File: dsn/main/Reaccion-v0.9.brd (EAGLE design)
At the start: 100 x 80 mm, 135 parts, among them J1 U.FL, Q1 2N7002K-T1-E3, Q3 2N7002K-T1-E3, Q9 SI2301CDS, T1 BC847, T2 BC847

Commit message: PCB re-design
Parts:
- removed C12: T491A336K004AT, custom_componentsv0.9:3216-18
- removed C13: EDK105M050A9BAA, custom_componentsv0.9:EDK105M050A9BAA
- removed C26, CS, CS1: 1uF, SparkFun-Capacitors:0805
- removed CF1, CF2, CF3: 39pF, SparkFun-Capacitors:0805
- removed D1, D2, D3: MBRS140T3-D, custom_componentsv0.9:MBRS140T3G
- removed IC_14: MAX7313AEG, maxim:QSOP24
- removed IC_2, IC_4, IC_5: LM2621, custom_componentsv0.9:R-PDSO-G8
- removed JP4: GPIO, SparkFun-Connectors:2X10
- removed JP5: POWER_JACKPTH, SparkFun-Connectors:POWER_JACK_PTH
- removed L4, L5, L7: NR4018T6R8M, custom_componentsv0.9:NR4018/NRS4018
- removed R29, R30, R31, R32, R33, R34, R35, R39, R40, R41, R48: 4.7K, SparkFun-Resistors:0805
- removed RF1, RF3, RF5: 150K, SparkFun-Resistors:0805
- removed RF2: 91K, SparkFun-Resistors:0805
- removed RF4: 50K, SparkFun-Resistors:0805
- removed RF6: 16K, SparkFun-Resistors:0805
- removed RFQ, RFQ1, RFQ2: 160K, SparkFun-Resistors:0805
- removed SJ4: SOLDERJUMPERNO, SparkFun-Retired:SJ_2S-NO
- removed SJ5, SJ6: SOLDERJUMPERTRACE, SparkFun-Retired:SJ_2S-TRACE
- added CIN, CIN1: 100uF, custom_componentsv0.9:1210-POLARIZED
- added DOUT, DOUT1: SD1206S040S2R0, custom_componentsv0.9:1206-POL
- added JP6: USB-B, SparkFun-Connectors:USB-B-PTH
- added R13: 30K, SparkFun-Resistors:0805
- added R14, R21: 10K, SparkFun-Resistors:0805
- added R15: 84.5K, SparkFun-Resistors:0805
- added U$1, U$2: LT1935ES5, custom_componentsv0.9:SOT23-5
- added U1: MIC5219 3.3V, SparkFun-PowerIC:SOT23-5
- BAT1: value (none) -> 3.7V
- C1: value T491A336K004AT -> 0.22uF; device custom_componentsv0.9:3216-18 -> SparkFun-Capacitors:0805
- C11: value T491A686K004AT -> 470pF; device custom_componentsv0.9:3216-18 -> SparkFun-Capacitors:0805
- C2: value T491A686K004AT -> 68pF; device custom_componentsv0.9:3216-18 -> SparkFun-Capacitors:0805
- C3: value EDK105M050A9BAA -> 22uF; device custom_componentsv0.9:EDK105M050A9BAA -> SparkFun-Capacitors:0805
- C4: value T491A686K004AT -> 0.22uF; device custom_componentsv0.9:3216-18 -> SparkFun-Capacitors:0805
- C5: value T491A336K004AT -> 68pF; device custom_componentsv0.9:3216-18 -> SparkFun-Capacitors:0805
- C6: value EDK105M050A9BAA -> 47uF; device custom_componentsv0.9:EDK105M050A9BAA -> SparkFun-Capacitors:0805
- L3, L6: value NR4018T6R8M -> 1.8uH; device custom_componentsv0.9:NR4018/NRS4018 -> inductor-bourns:SRR4028
- R1, R2: value 500 -> 10K
- moved C11 20.8 mm to (21.6, 34.0), turned to 90 degrees
- moved C1 18.7 mm to (31.5, 15.6), turned to 0 degrees
- moved C4 16.4 mm to (12.9, 29.7), turned to 90 degrees
- moved C3 15.4 mm to (29.5, 4.80), turned to 180 degrees
- moved L3 13.7 mm to (23.4, 7.00), turned to 90 degrees
- moved IC_17 13.5 mm to (44.9, 53.4), flipped to the top
- moved IC_10 12.0 mm to (81.4, 34.0)
- moved L6 11.5 mm to (21.6, 21.6), turned to 180 degrees
- moved IC_18 11.2 mm to (32.6, 53.3), flipped to the top
- moved C6 10.8 mm to (23.8, 27.5), turned to 270 degrees
- moved S1 10.0 mm to (50.0, 40.0)
- moved D4 9.68 mm to (11.6, 14.1), turned to 0 degrees
- moved C19 9.51 mm to (18.4, 66.0)
- moved C2 9.29 mm to (31.5, 11.7), turned to 180 degrees
- moved R42 9.23 mm to (45.9, 40.2), turned to 270 degrees
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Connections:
- removed net 1V8_EN: IC_13.18, IC_3.3, R34.2
- removed net 1V8_TRANS_EN: IC_13.19, IC_17.8, IC_18.8, R33.2
- removed net 2V8_TRANS_EN: IC_10.8, IC_13.20, R32.2
- removed net BT_RESET: IC_13.5, IC_15.11, R40.2
- removed net GPIO1: IC_14.5, JP4.3
- removed net GPIO10: IC_14.15, JP4.13
- removed net GPIO11: IC_14.16, JP4.14
- removed net GPIO12: IC_14.17, JP4.15
- removed net GPIO13: IC_14.18, JP4.16
- removed net GPIO14: IC_14.19, JP4.17
- removed net GPIO15: IC_14.20, JP4.18
- removed net GPIO2: IC_14.6, JP4.5
- removed net GPIO3: IC_14.7, JP4.6
- removed net GPIO4: IC_14.8, JP4.7
- removed net GPIO5: IC_14.9, JP4.8
- removed net GPIO6: IC_14.10, JP4.9
- removed net GPIO7: IC_14.11, JP4.10
- removed net GPIO8: IC_14.13, JP4.11
- removed net GPIO9: IC_14.14, JP4.12
- removed net IO_INT1: IC_12.33, IC_14.1
- removed net N$10: CS1.2, D2.1, L7.P$2
- removed net N$16: IC_5.3, RFQ2.1
- removed net N$17: CF3.1, IC_5.4, RF5.2, RF6.1
- removed net N$40: IC_14.21, R29.1, SJ4.2
- removed net N$41: IC_14.2, R30.1, SJ5.2
- removed net N$42: IC_14.3, R31.1, SJ6.2
- removed net N$7: CS.2, D1.1, L4.P$2
- removed net N$9: CF2.1, IC_4.4, RF3.2, RF4.1
- removed net W: C20.2, R18.2
- net 12V: now also C2.1, C3.1, DOUT1.2, R15.1; no longer C11.1, CF3.2, D3.2, RF5.1
- net 12V_EN: now also IC_12.26, R1.1; no longer IC_5.2, R35.2
- net 3V3: now also U1.5; no longer C2.1, C26.2, CF1.2, D1.2, IC_10.14, IC_14.24, IC_17.14, IC_18.14, IC_3.1, JP1.9, JP2.1, JP4.4, R29.2, R3.2, R30.2, R31.2, R32.1, R33.1, R34.1, R35.1, R39.1, R40.1, R41.1, R48.1, R5.2, RF1.1
- net 5V: now also C5.1, C6.1, DOUT.2, IC_10.14, IC_10.8, IC_17.14, IC_17.8, IC_18.14, IC_18.8, IC_3.1, IC_3.3, JP1.9, JP2.1, R13.1, R3.2, R5.2, U1.1, U1.3; no longer C4.1, C7.2, CF2.2, D2.2, IC_6.4, JP4.1, JP4.2, RF3.1
- net BT_CMD: now also IC_12.33, IC_15.26; no longer IC_13.6, R39.2
- net BT_EN: now also IC_12.27; no longer IC_13.4, R41.2
- net GND: now also C11.1, C3.2, C6.2, CIN.2, CIN1.2, JP6.GND, R14.2, R21.2, U$1.2, U$2.2, U1.2; no longer C11.2, C12.2, C13.P$2, C2.2, C26.1, C3.P$2, C5.2, C6.P$2, IC_14.12, IC_2.1, IC_2.5, IC_4.1, IC_4.5, IC_5.1, IC_5.5, JP4.19, JP4.20, JP5.GND, JP5.GNDBREAK, L4.P$1, L7.P$1, RF2.2, RF4.2, RF6.2, SJ4.1, SJ5.1, SJ6.1
- net N$1: now also DOUT1.1, L3.2, U$2.1; no longer CS.1, IC_2.8, L3.P$2
- net N$14: now also IC_12.29; no longer D3.1, IC_5.8, L5.P$2
- net N$2: now also DOUT.1, L6.2, U$1.1; no longer CS1.1, IC_4.8, L6.P$2
- net N$3: now also C1.1, R1.2, U$2.4; no longer C3.P$1, IC_2.2, IC_2.6, R1.1, RFQ.2
- net N$4: now also C11.2, U1.4; no longer IC_2.3, RFQ.1
- net N$5: now also C2.2, R15.2, R21.1, U$2.3; no longer CF1.1, IC_2.4, RF1.2, RF2.1
- net N$6: now also C5.2, R13.2, R14.1, U$1.3; no longer C6.P$1, IC_4.2, IC_4.6, R2.1, RFQ1.2
- net N$8: now also C4.1, R2.2, U$1.4; no longer IC_4.3, RFQ1.1
- net SCL: no longer IC_14.22
- net SDA: no longer IC_14.23
- net SIM_DATA: now also C20.2, R18.2
- net VEXT: now also C7.2, IC_6.4, JP6.VBUS; no longer JP5.PWR
- net VIN: now also CIN.1, CIN1.1, L3.1, L6.1, R2.1, U$1.5, U$2.5; no longer C1.1, C12.1, C13.P$1, C5.1, IC_2.7, IC_4.7, IC_5.6, IC_5.7, L3.P$1, L5.P$1, L6.P$1, R1.2, R2.2, RFQ2.2
- net XBEE_RESET: now also IC_12.28; no longer IC_14.4, R48.2
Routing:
- net GND: track 8.37 -> 1008.3 mm, vias 72 -> 45
- net 3V3: track 437.5 -> 206.5 mm, vias 14 -> 9
- net 5V: track 103.8 -> 275.9 mm, vias 4 -> 5
- net 1V8_TRANS_EN: track 149.2 -> 0.00 mm, vias 9 -> 0
- net 1V8_EN: track 147.3 -> 0.00 mm, vias 8 -> 0
- net SIM_DATA: track 0.00 -> 75.4 mm, vias 0 -> 5
- net W: track 63.5 -> 0.00 mm, vias 3 -> 0
- net BT_RESET: track 55.5 -> 0.00 mm, vias 4 -> 0
- net VIN: track 112.5 -> 57.0 mm
- net 2V8_TRANS_EN: track 49.9 -> 0.00 mm, vias 6 -> 0
- net 12V: track 104.1 -> 142.6 mm, vias 2 -> 5
- net IO_INT1: track 28.3 -> 0.00 mm, vias 2 -> 0
- net SIM900_PWR: track 83.0 -> 55.7 mm
- net SCL: track 105.7 -> 81.8 mm, vias 7 -> 3
- net SPI1_MISO: track 60.4 -> 37.0 mm, vias 1 -> 0
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- added copper zone on layer 1, net N$2
- removed copper zone on layer 16, net GND

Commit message: Laen's DRC corrections, small modifications
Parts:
- JP2: device SparkFun-Connectors:AVR_ICSP -> pinhead:2X05
- turned JP2 to 270 degrees
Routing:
- net N$37: track 7.29 -> 13.2 mm
- net SDA: track 75.8 -> 77.0 mm
- added copper zone on layer 16, net GND

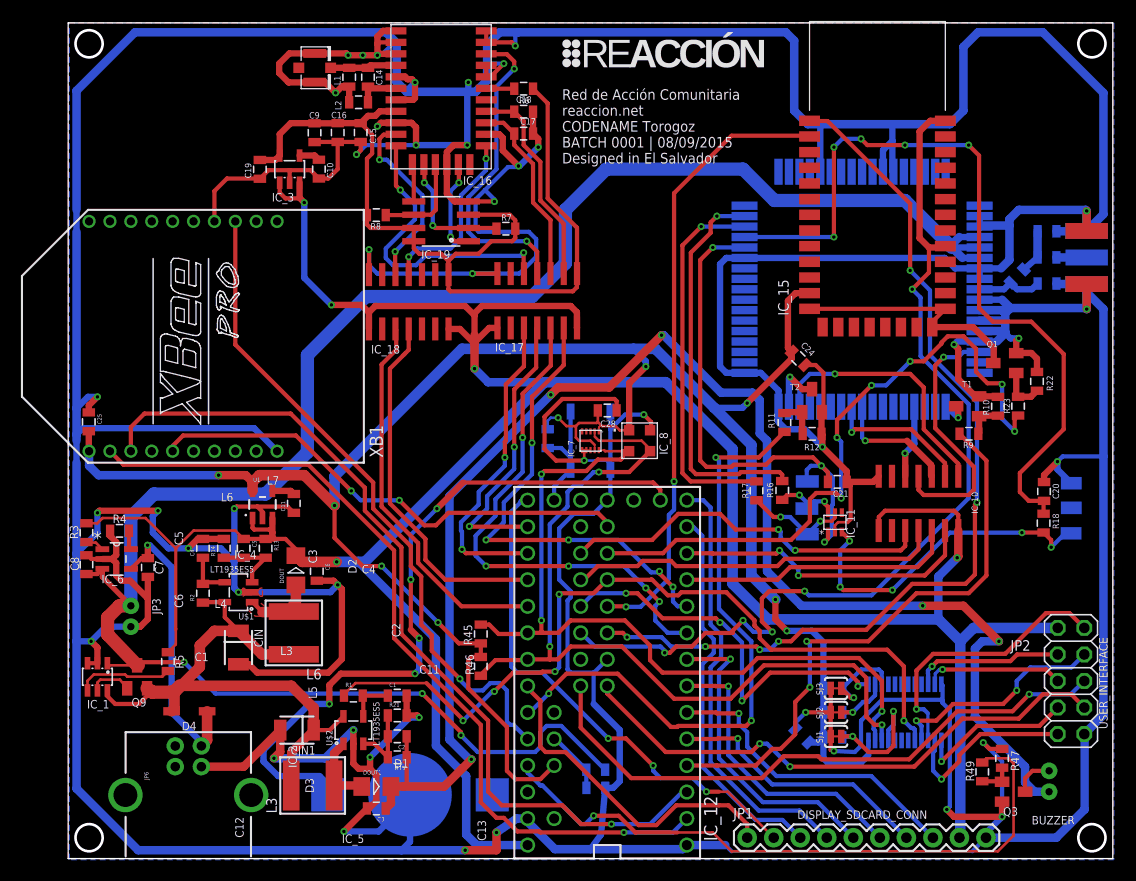
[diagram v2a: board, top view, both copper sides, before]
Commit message: Added power source corrections
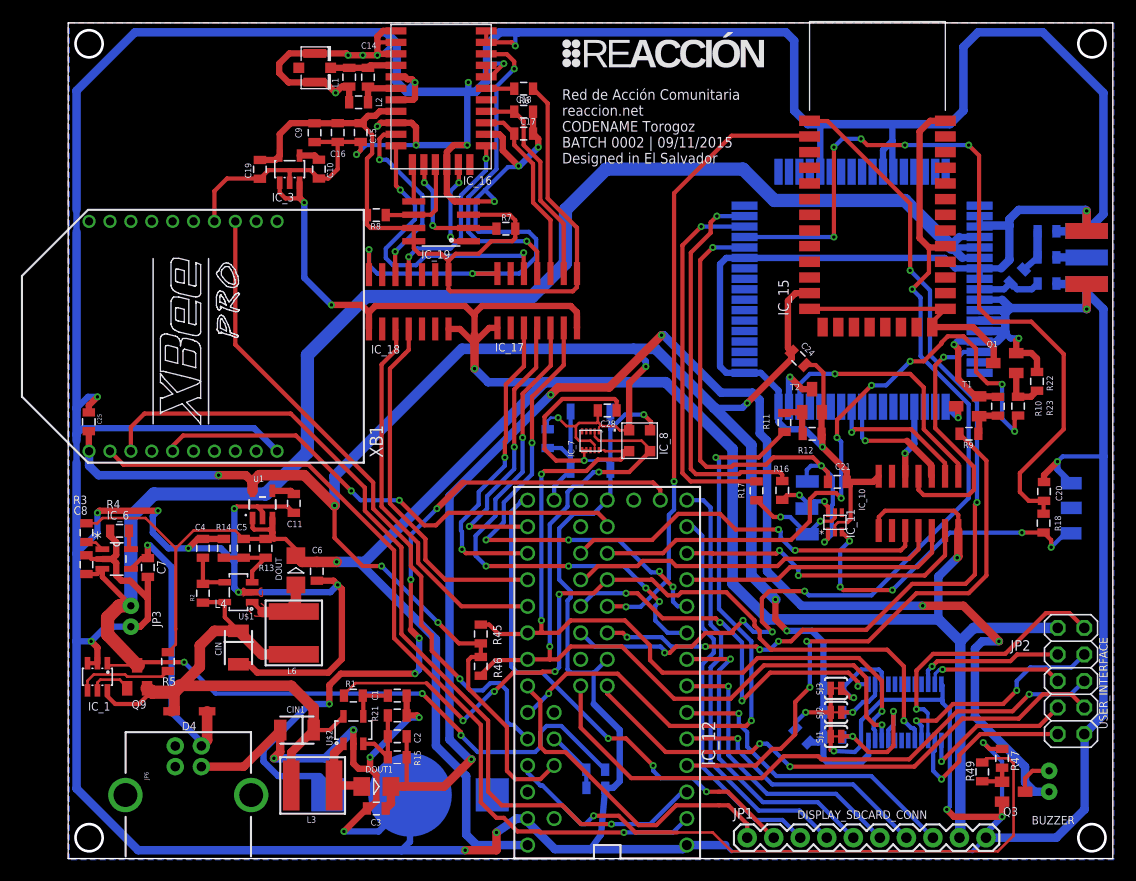
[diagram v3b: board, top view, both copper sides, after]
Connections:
- removed net N$14: IC_12.29
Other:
- board text added: "Red de Acción Comunitaria reaccion.net CODENAME Torogoz BATCH 0002 | 09/11/2015 Designed in El Salvador"
- board text removed: "C1"
- board text removed: "C11"
- board text removed: "C12"
- board text removed: "C13"
- board text removed: "C2"
- board text removed: "C3"
- board text removed: "C4"
- board text removed: "C5"
- board text removed: "C6"
- board text removed: "D1"
- board text removed: "D2"
- board text removed: "D3"
- board text removed: "IC_2"
- board text removed: "IC_4"
- board text removed: "IC_5"
- board text removed: "L3"
- board text removed: "L5"
- board text removed: "L6"
- board text removed: "L7"
- board text removed: "Red de Acción Comunitaria reaccion.net CODENAME Torogoz BATCH 0001 | 08/09/2015 Designed in El Salvador"

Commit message: Initial release for Prototipo1
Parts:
- IC_7: device Reaccion-Custom:2X2-DFN -> Reaccion-Custom-revised:2X2-DFN
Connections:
- net 3V3: now also IC_7.8; no longer IC_7.9
- net BT_RX: now also IC_12.21/A7; no longer IC_12.25
- net BT_TX: now also IC_12.20/A6; no longer IC_12.24
- net CHG_STAT: now also IC_13.5
- net DISPLAY_BL: now also IC_12.24; no longer IC_12.20/A6
- net GND: now also IC_7.9; no longer IC_7.8
- net PWR_STAT: now also IC_13.4
- net SIM900_RESET: now also IC_12.25; no longer IC_12.21/A7
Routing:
- net DISPLAY_BL: track 32.1 -> 8.85 mm
- net SIM900_RESET: track 59.5 -> 49.3 mm, vias 3 -> 2
- net BT_TX: track 90.0 -> 84.6 mm, vias 6 -> 5
- net BT_RX: track 60.6 -> 57.4 mm, vias 2 -> 1
- net GND: track 1008.7 -> 1009.9 mm
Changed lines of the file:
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@@
 <setting verticaltext="up"/>
 </settings>
-<grid distance="0.1" unitdist="mm" unit="mm" style="lines" multiple="1" display="yes" altdistance="0.1" altunitdist="mm" altunit="mm"/>
+<grid distance="0.01" unitdist="mm" unit="mm" style="lines" multiple="1" display="yes" altdistance="0.01" altunitdist="mm" altunit="mm"/>
 <layers>
 <layer number="1" name="Top" color="4" fill="1" visible="yes" active="yes"/>
@@
 <attribute name="NAME" x="57.41" y="38.67" size="0.8128" layer="25" font="fixed" rot="R90"/>
 </element>
-<element name="IC_7" library="Reaccion-Custom" package="2X2-DFN" value="MMA8653FC" x="50" y="40" smashed="yes" rot="R270">
+<element name="IC_7" library="Reaccion-Custom-revised" package="2X2-DFN" value="MMA8653FC" x="50" y="40" smashed="yes" rot="R270">
 <attribute name="NAME" x="48.45" y="38.44" size="0.6096" layer="21" font="fixed" rot="R90"/>
 </element>
@@
 <contactref element="R47" pad="1"/>
 <contactref element="Q3" pad="2"/>
-<contactref element="IC_7" pad="8"/>
+<contactref element="IC_7" pad="9"/>
 <contactref element="IC_7" pad="7"/>
 <contactref element="IC_7" pad="6"/>
@@
 <wire x1="49.4" y1="38.9025" x2="49.2" y2="39.1025" width="0.254" layer="1"/>
 <wire x1="49.6" y1="39.1025" x2="49.2" y2="39.1025" width="0.254" layer="1"/>
-<wire x1="50" y1="39.1025" x2="49.6" y2="39.1025" width="0.1524" layer="1"/>
 <wire x1="51.905" y1="42.794" x2="51.905" y2="41.1" width="0.4064" layer="16"/>
 <wire x1="51.905" y1="41.1" x2="51.905" y2="37.7" width="0.4064" layer="16"/>
@@
 <wire x1="77.9" y1="15.2" x2="83.6" y2="15.2" width="0.4064" layer="16"/>
 <wire x1="83.6" y1="15.2" x2="83.7" y2="15.1" width="0.4064" layer="16"/>
+<wire x1="50.4" y1="39.1025" x2="50.4" y2="38.77" width="0.1524" layer="1"/>
+<wire x1="50.4" y1="38.77" x2="49.73" y2="38.1" width="0.1524" layer="1"/>
+<wire x1="49.73" y1="38.1" x2="49.4" y2="38.1" width="0.1524" layer="1"/>
 </signal>
 <signal name="VIN">
@@
 <contactref element="R42" pad="1"/>
 <contactref element="IC_7" pad="1"/>
-<contactref element="IC_7" pad="9"/>
+<contactref element="IC_7" pad="8"/>
 <contactref element="IC_8" pad="1"/>
 <contactref element="C25" pad="2"/>
@@
 <wire x1="50.7" y1="42.9" x2="50.7" y2="41.8" width="0.254" layer="1"/>
 <wire x1="50.7" y1="41.8" x2="51.1" y2="41.4" width="0.254" layer="1"/>
-<wire x1="50.4" y1="39.1025" x2="50.4" y2="39.6" width="0.1524" layer="1"/>
-<wire x1="50.4" y1="39.6" x2="50" y2="40" width="0.254" layer="1"/>
-<wire x1="50" y1="40" x2="48.9" y2="40" width="0.254" layer="1"/>
 <wire x1="48.9" y1="40" x2="48.6" y2="40.3" width="0.254" layer="1"/>
 <wire x1="48.6" y1="40.3" x2="48.6" y2="41.4" width="0.254" layer="1"/>
@@
 <wire x1="71.2" y1="21.8" x2="72.3" y2="20.7" width="0.6096" layer="16"/>
 <wire x1="72.3" y1="20.7" x2="72.3" y2="16.3" width="0.6096" layer="16"/>
+<wire x1="48.9" y1="40" x2="49.7" y2="40" width="0.254" layer="1"/>
+<wire x1="49.7" y1="40" x2="50" y2="39.7" width="0.1524" layer="1"/>
+<wire x1="50" y1="39.7" x2="50" y2="39.1025" width="0.1524" layer="1"/>
 </signal>
 <signal name="5V">
@@
 <wire x1="3.270853125" y1="29.61825625" x2="2.651771875" y2="30.2373375" width="0.254" layer="1"/>
 <wire x1="2.651771875" y1="30.2373375" x2="1.75" y2="30.3" width="0.254" layer="1"/>
+<contactref element="IC_13" pad="5"/>
+<wire x1="3.270853125" y1="29.61825625" x2="79.1475" y2="16.69" width="0" layer="19" extent="1-16"/>
 </signal>
 <signal name="N$11">
@@
 <wire x1="5.65" y1="17.42" x2="9.01500625" y2="17.42" width="0.254" layer="1"/>
 <wire x1="9.01500625" y1="17.42" x2="9.55" y2="17.95499375" width="0.254" layer="1"/>
+<contactref element="IC_13" pad="4"/>
+<wire x1="9.55" y1="17.95499375" x2="78.5125" y2="16.69" width="0" layer="19" extent="1-16"/>
 </signal>
 <signal name="N$13">
@@
 <signal name="SIM900_RESET">
 <contactref element="R11" pad="1"/>
-<contactref element="IC_12" pad="21/A7"/>
-<wire x1="43.98" y1="13.99" x2="44.19" y2="13.99" width="0.4064" layer="16"/>
-<wire x1="44.19" y1="13.99" x2="46" y2="15.8" width="0.4064" layer="16"/>
-<via x="46" y="15.8" extent="1-16" drill="0.3302"/>
-<wire x1="46" y1="15.8" x2="46" y2="16" width="0.4064" layer="1"/>
-<wire x1="46" y1="16" x2="47.7" y2="17.7" width="0.4064" layer="1"/>
-<wire x1="47.7" y1="17.7" x2="52.6" y2="17.7" width="0.4064" layer="1"/>
 <wire x1="57.6" y1="12.7" x2="64.9" y2="12.7" width="0.4064" layer="1"/>
 <wire x1="64.9" y1="12.7" x2="65.4" y2="13.2" width="0.4064" layer="1"/>
@@
 <wire x1="66.115759375" y1="38.4" x2="68.564346875" y2="40.8485875" width="0.4064" layer="1"/>
 <wire x1="52.6" y1="17.7" x2="57.6" y2="12.7" width="0.4064" layer="1"/>
+<contactref element="IC_12" pad="25"/>
+<wire x1="52.6" y1="17.7" x2="51.6" y2="24.15" width="0" layer="19" extent="1-1"/>
 </signal>
 <signal name="SIM900_PWR">
@@
 <signal name="BT_TX">
 <contactref element="IC_15" pad="1"/>
-<contactref element="IC_12" pad="24"/>
-<wire x1="51.6" y1="21.61" x2="53.09" y2="21.61" width="0.4064" layer="1"/>
-<wire x1="53.09" y1="21.61" x2="53.5" y2="21.2" width="0.4064" layer="1"/>
-<via x="53.5" y="21.2" extent="1-16" drill="0.3302"/>
-<wire x1="53.5" y1="21.2" x2="56.8" y2="21.2" width="0.4064" layer="16"/>
 <wire x1="56.8" y1="21.2" x2="57.7" y2="20.3" width="0.4064" layer="16"/>
 <wire x1="57.7" y1="20.3" x2="61" y2="20.3" width="0.4064" layer="16"/>
@@
 <wire x1="82.5" y1="54.4" x2="82.5" y2="48.2" width="0.4064" layer="16"/>
 <wire x1="82.5" y1="48.2" x2="87" y2="43.7" width="0.4064" layer="16"/>
+<contactref element="IC_12" pad="20/A6"/>
+<wire x1="43.98" y1="16.53" x2="56.8" y2="21.2" width="0" layer="19" extent="16-16"/>
 </signal>
 <signal name="BT_RX">
 <contactref element="IC_15" pad="2"/>
-<contactref element="IC_12" pad="25"/>
-<wire x1="51.6" y1="24.15" x2="53.35" y2="24.15" width="0.4064" layer="1"/>
-<wire x1="53.35" y1="24.15" x2="53.4" y2="24.1" width="0.4064" layer="1"/>
-<via x="53.4" y="24.1" extent="1-16" drill="0.3302"/>
-<wire x1="53.4" y1="24.1" x2="54.8" y2="24.1" width="0.4064" layer="16"/>
 <wire x1="54.8" y1="24.1" x2="57.5" y2="26.8" width="0.4064" layer="16"/>
 <wire x1="57.5" y1="26.8" x2="57.5" y2="32.9" width="0.4064" layer="16"/>
@@
 <wire x1="71.5" y1="69" x2="71.09625" y2="69" width="0.4064" layer="1"/>
 <wire x1="71.09625" y1="69" x2="70.969915625" y2="69.126334375" width="0.4064" layer="1"/>
+<contactref element="IC_12" pad="21/A7"/>
+<wire x1="43.98" y1="13.99" x2="54.8" y2="24.1" width="0" layer="19" extent="16-16"/>
 </signal>
 <signal name="BT_CMD">
@@
 <signal name="DISPLAY_BL">
 <contactref element="JP1" pad="1"/>
-<contactref element="IC_12" pad="20/A6"/>
-<wire x1="43.98" y1="16.53" x2="43.98" y2="16.32" width="0.4064" layer="1"/>
-<wire x1="43.98" y1="16.32" x2="45.2" y2="15.1" width="0.4064" layer="1"/>
-<wire x1="45.2" y1="15.1" x2="45.2" y2="10.7" width="0.4064" layer="1"/>
-<wire x1="45.2" y1="10.7" x2="45.7" y2="10.2" width="0.4064" layer="1"/>
-<wire x1="45.7" y1="10.2" x2="47.6" y2="10.2" width="0.4064" layer="1"/>
-<wire x1="47.6" y1="10.2" x2="54.6" y2="3.2" width="0.4064" layer="1"/>
-<wire x1="54.6" y1="3.2" x2="56.3" y2="3.2" width="0.4064" layer="1"/>
-<wire x1="56.3" y1="3.2" x2="58.2" y2="5.1" width="0.4064" layer="1"/>
-<wire x1="58.2" y1="5.1" x2="62.3" y2="5.1" width="0.4064" layer="1"/>
-<wire x1="62.3" y1="5.1" x2="63.2" y2="5.1" width="0.4064" layer="1"/>
+<wire x1="58.2" y1="5.1" x2="63.2" y2="5.1" width="0.4064" layer="1"/>
 <wire x1="63.2" y1="5.1" x2="65" y2="3.3" width="0.4064" layer="1"/>
 <wire x1="65" y1="3.3" x2="65" y2="2" width="0.4064" layer="1"/>
+<contactref element="IC_12" pad="24"/>
+<wire x1="58.2" y1="5.1" x2="51.6" y2="21.61" width="0" layer="19" extent="1-1"/>
 </signal>
 <signal name="SPI1_SCK">
